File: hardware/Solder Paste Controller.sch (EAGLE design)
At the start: 42 parts, among them U1 ATMEGA328P_TQFP, U2 AMS1117, U3 AO3401, U4 ULN2003

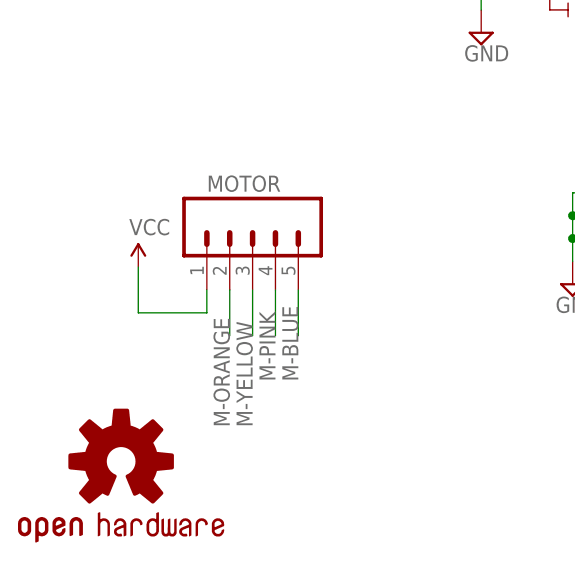
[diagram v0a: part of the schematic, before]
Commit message: added mounting holes
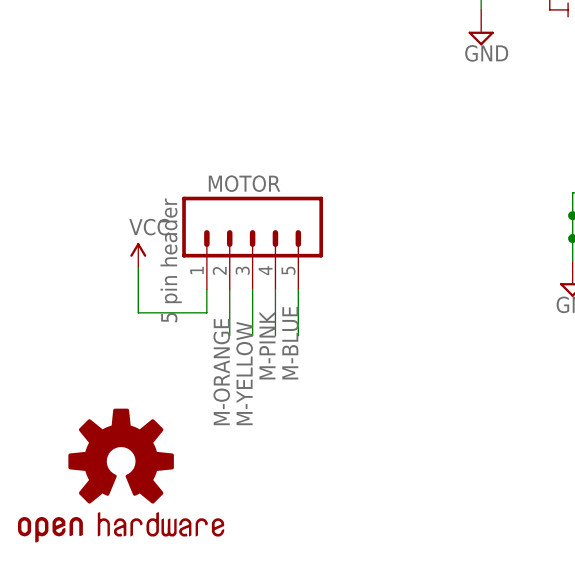
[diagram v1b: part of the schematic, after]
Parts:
- DC-IN: value POWER-IN-WITH-RELIEF -> red black twister wire
- FTDI: value (none) -> 6 pin header
- MOTOR: value (none) -> 5 pin header
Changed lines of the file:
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@@
 <setting verticaltext="up"/>
 </settings>
-<grid distance="10" unitdist="mil" unit="mil" style="lines" multiple="1" display="no" altdistance="0.01" altunitdist="inch" altunit="inch"/>
+<grid distance="0.1" unitdist="inch" unit="inch" style="lines" multiple="1" display="no" altdistance="0.01" altunitdist="inch" altunit="inch"/>
 <layers>
 <layer number="1" name="Top" color="4" fill="1" visible="no" active="no"/>
@@
 <part name="CRYSTAL" library="ELK LABS" deviceset="CSTCE16M0V53-R0" device=""/>
 <part name="SUPPLY9" library="supply2" deviceset="GND" device=""/>
-<part name="DC-IN" library="ELK LABS" deviceset="POWER-IN-WITH-RELIEF" device=""/>
+<part name="DC-IN" library="ELK LABS" deviceset="POWER-IN-WITH-RELIEF" device="" value="red black twister wire"/>
 <part name="SUPPLY10" library="supply2" deviceset="GND" device=""/>
 <part name="U4" library="ELK LABS" deviceset="ULN2003" device=""/>
@@
 <part name="SUPPLY21" library="supply2" deviceset="GND" device=""/>
 <part name="AVR-ISP" library="adafruit" deviceset="AVRISP" device="-6"/>
-<part name="FTDI" library="SparkFun-Connectors" deviceset="ARDUINO_SERIAL_PROGRAM" device="PTH"/>
+<part name="FTDI" library="SparkFun-Connectors" deviceset="ARDUINO_SERIAL_PROGRAM" device="PTH" value="6 pin header"/>
 <part name="SUPPLY24" library="supply2" deviceset="GND" device=""/>
 <part name="VCC3" library="SparkFun-Aesthetics" deviceset="VCC" device=""/>
@@
 <part name="VCC4" library="SparkFun-Aesthetics" deviceset="VCC" device=""/>
 <part name="VCC6" library="SparkFun-Aesthetics" deviceset="VCC" device=""/>
-<part name="MOTOR" library="SparkFun-Connectors" deviceset="M05" device="PTH"/>
+<part name="MOTOR" library="SparkFun-Connectors" deviceset="M05" device="PTH" value="5 pin header"/>
 <part name="VCC5" library="SparkFun-Aesthetics" deviceset="VCC" device=""/>
 <part name="U$1" library="ELK LABS" deviceset="ELK-LOGO" device=""/>
@@
 </instance>
 <instance part="FTDI" gate="G$1" x="238.76" y="71.12" smashed="yes" rot="R270">
-<attribute name="VALUE" x="228.6" y="76.2" size="1.778" layer="96" rot="R270"/>
 <attribute name="NAME" x="237.49" y="79.502" size="1.778" layer="95"/>
 </instance>
